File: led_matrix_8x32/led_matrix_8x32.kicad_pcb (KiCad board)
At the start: 2 copper layers, 263 parts, among them IC1 IS31FL3731-QFLS2-TR, IC2 IS31FL3731-QFLS2-TR, J1 Conn_01x04_Female

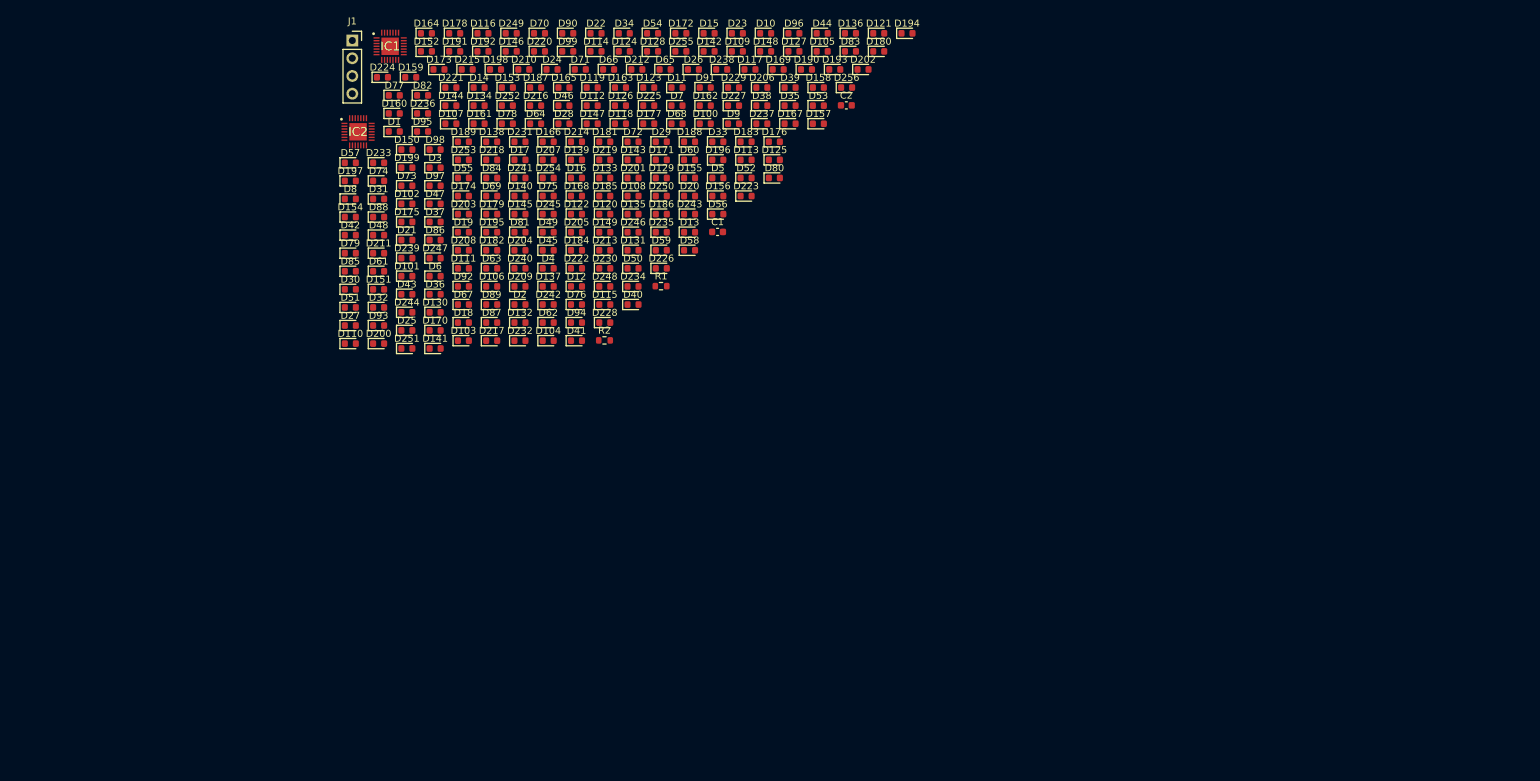
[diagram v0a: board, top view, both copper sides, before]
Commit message: complete hald of led matrix pcb layout
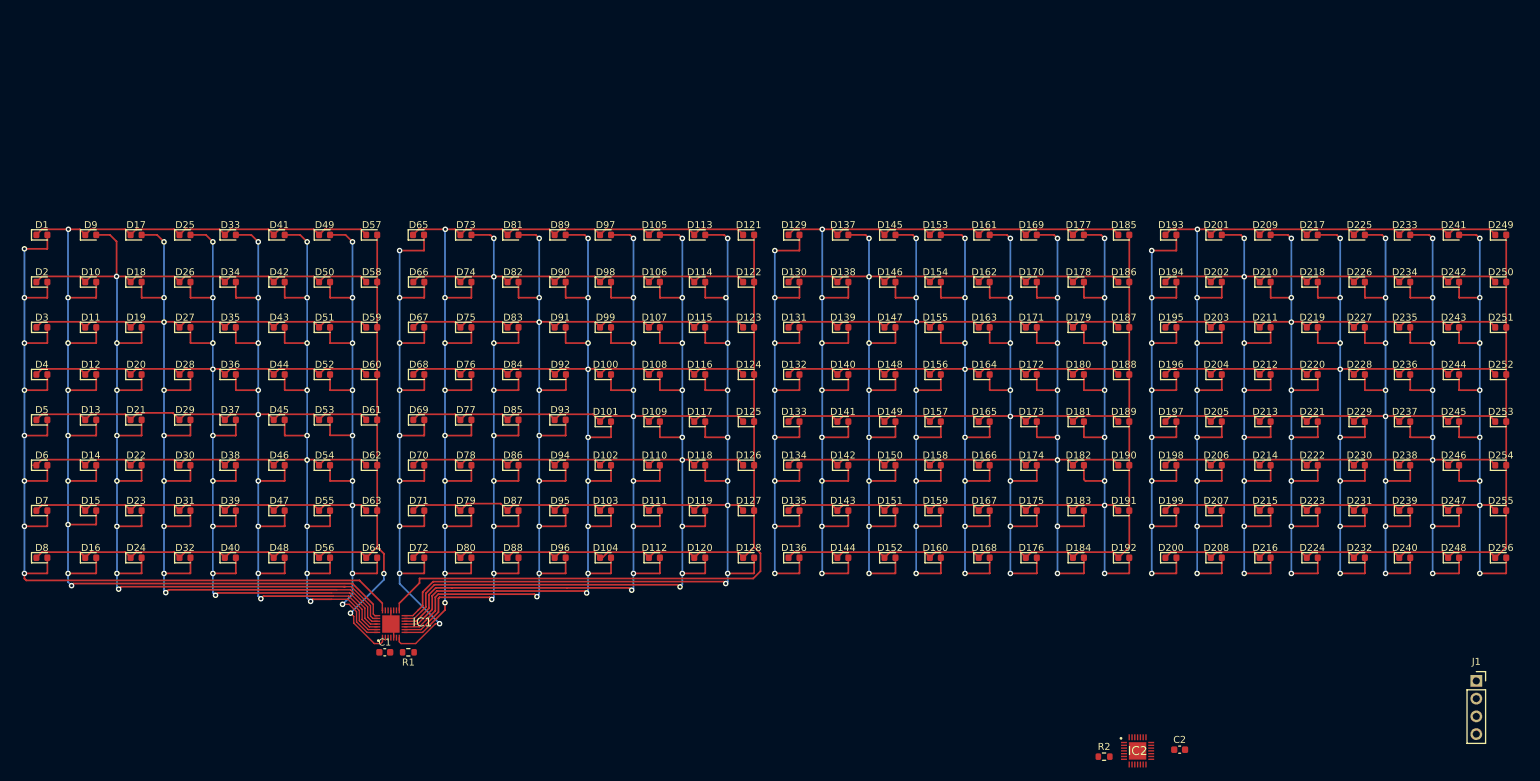
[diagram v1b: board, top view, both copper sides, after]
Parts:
- moved J1 185.3 mm to (241.5, 137.9)
- moved D251 156.7 mm to (245.0, 87.2)
- moved D253 153.3 mm to (245.0, 100.8)
- moved D247 150.3 mm to (238.2, 113.5)
- moved D244 150.2 mm to (238.2, 94.0)
- moved D224 149.9 mm to (218.0, 120.2)
- moved D239 147.5 mm to (231.2, 113.5)
- moved D252 147.4 mm to (245.0, 94.0)
- moved D233 147.4 mm to (231.2, 74.0)
- moved D236 145.6 mm to (231.2, 94.0)
- moved D249 144.7 mm to (245.0, 74.0)
- moved IC2 142.6 mm to (193.0, 147.9)
- moved D254 142.5 mm to (245.0, 107.0)
- moved D255 134.6 mm to (245.0, 113.5)
- moved D241 134.0 mm to (238.2, 74.0)
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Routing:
- net /CA2_1: track 0.00 -> 193.7 mm, vias 0 -> 9
- net /CB8_1: track 0.00 -> 187.8 mm, vias 0 -> 9
- net /CB7_1: track 0.00 -> 181.2 mm, vias 0 -> 9
- net /CA3_1: track 0.00 -> 180.1 mm, vias 0 -> 8
- net /CB6_1: track 0.00 -> 176.4 mm, vias 0 -> 9
- net /CA4_1: track 0.00 -> 174.8 mm, vias 0 -> 9
- net /CB5_1: track 0.00 -> 168.7 mm, vias 0 -> 9
- net /CA5_1: track 0.00 -> 165.7 mm, vias 0 -> 9
- net /CB4_1: track 0.00 -> 164.3 mm, vias 0 -> 9
- net /CA6_1: track 0.00 -> 161.3 mm, vias 0 -> 9
- net /CB9_1: track 0.00 -> 157.9 mm
- net /CB3_1: track 0.00 -> 157.7 mm, vias 0 -> 9
- net /CB2_1: track 0.00 -> 156.0 mm, vias 0 -> 9
- net /CA7_1: track 0.00 -> 153.1 mm, vias 0 -> 9
- net /CA8_1: track 0.00 -> 148.9 mm, vias 0 -> 9
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
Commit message: add led matrix gerbers (jlcpcb)
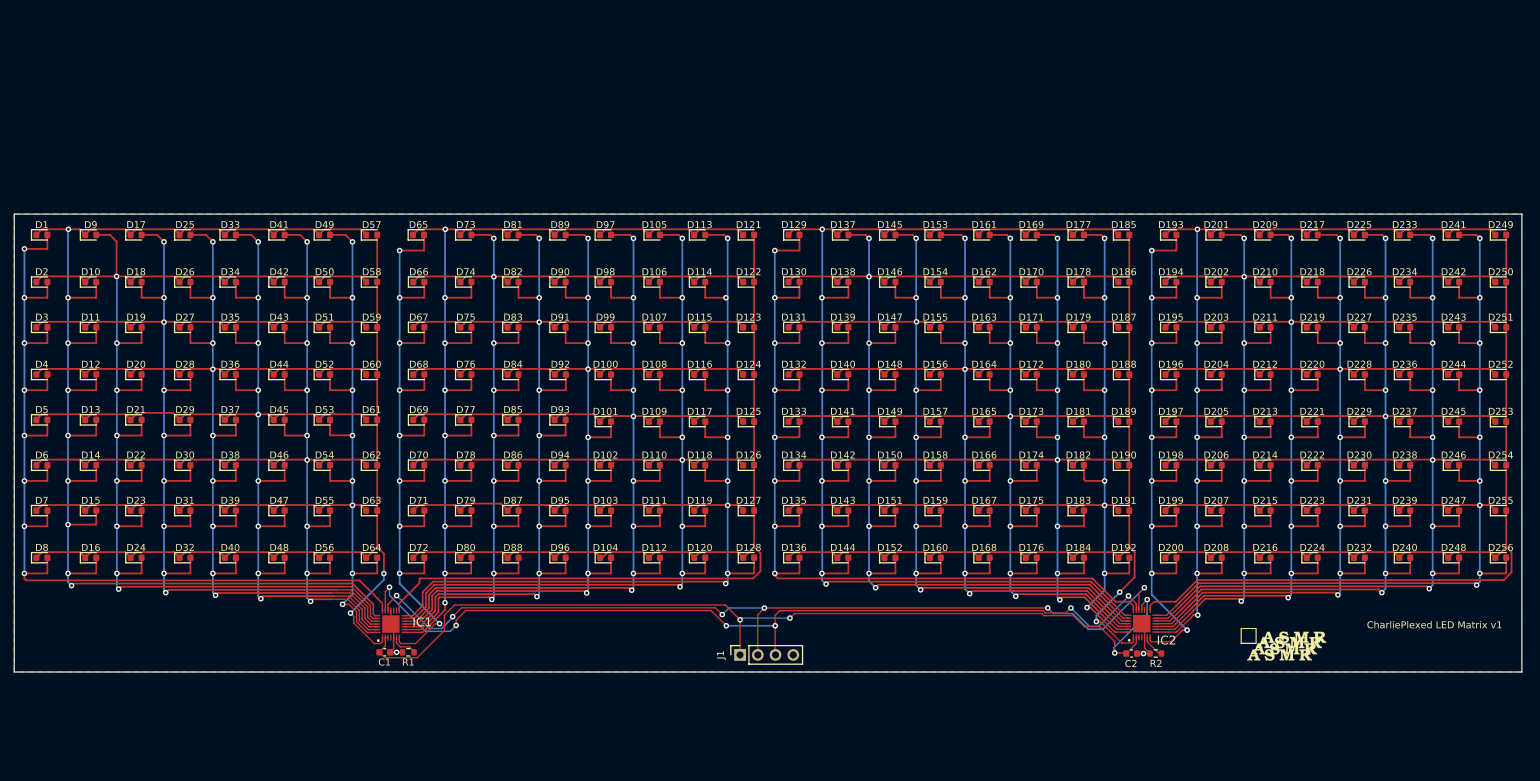
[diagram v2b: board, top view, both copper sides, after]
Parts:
- added G***: LOGO, ASMR_footprints:SilkScreen_asmrrrrrrrrr, F.Cu at (213.9, 132.9)
- moved J1 105.5 mm to (136.0, 134.2), turned to 90 degrees
- moved IC2 18.2 mm to (193.6, 129.7), turned to 90 degrees
- moved R2 16.5 mm to (195.6, 134.0), turned to 180 degrees
- moved C2 15.4 mm to (192.1, 134.0)
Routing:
- net +5V: track 0.00 -> 139.1 mm, vias 0 -> 4
- net /SDA: track 0.00 -> 128.2 mm, vias 0 -> 6
- net /SCL: track 0.00 -> 127.1 mm, vias 0 -> 6
- net /CB9_2: track 99.0 -> 157.4 mm
- net /CA1_2: track 92.4 -> 146.4 mm
- net /CB8_2: track 135.3 -> 185.2 mm, vias 8 -> 9
- net /CA2_2: track 143.5 -> 190.7 mm, vias 8 -> 9
- net /CB7_2: track 137.4 -> 181.0 mm, vias 8 -> 9
- net /CA3_2: track 139.4 -> 180.2 mm, vias 8 -> 9
- net /CB6_2: track 136.2 -> 173.6 mm, vias 8 -> 9
- net /CA4_2: track 137.3 -> 171.8 mm, vias 8 -> 9
- net /CB5_2: track 137.5 -> 168.9 mm, vias 8 -> 9
- net /CA5_2: track 138.3 -> 166.2 mm, vias 8 -> 9
- net /CB4_2: track 138.6 -> 163.2 mm, vias 8 -> 9
- net /CA6_2: track 136.9 -> 158.7 mm, vias 8 -> 9
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- added copper zone on B.Cu, net GND
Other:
- board outline added: 216 x 65.6 mm
- board text added: "CharliePlexed LED Matrix v1"
